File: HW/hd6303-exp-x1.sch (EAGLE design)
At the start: 40 parts, among them IC1 74HC245N, IC2 74HC245N, IC3 74HC245N, IC4 LM386N-1

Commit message: pullup for page_a13-page_a17, fixed decoder rom
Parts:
- C1, C10, C3, C4, C5, C6, C7, C8, C9: value (none) -> 100n
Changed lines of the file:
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@@
 <part name="GND10" library="supply1" library_urn="urn:adsk.eagle:library:371" deviceset="GND" device=""/>
 <part name="R3" library="resistor" library_urn="urn:adsk.eagle:library:348" deviceset="R-EU_" device="R0603" package3d_urn="urn:adsk.eagle:package:26057/1" value="10k"/>
-<part name="C4" library="rcl" deviceset="C-EU" device="C0603"/>
-<part name="C5" library="rcl" deviceset="C-EU" device="C0603"/>
-<part name="C6" library="rcl" deviceset="C-EU" device="C0603"/>
-<part name="C7" library="rcl" deviceset="C-EU" device="C0603"/>
-<part name="C8" library="rcl" deviceset="C-EU" device="C0603"/>
-<part name="C9" library="rcl" deviceset="C-EU" device="C0603"/>
-<part name="C10" library="rcl" deviceset="C-EU" device="C0603"/>
+<part name="C4" library="rcl" deviceset="C-EU" device="C0603" value="100n"/>
+<part name="C5" library="rcl" deviceset="C-EU" device="C0603" value="100n"/>
+<part name="C6" library="rcl" deviceset="C-EU" device="C0603" value="100n"/>
+<part name="C7" library="rcl" deviceset="C-EU" device="C0603" value="100n"/>
+<part name="C8" library="rcl" deviceset="C-EU" device="C0603" value="100n"/>
+<part name="C9" library="rcl" deviceset="C-EU" device="C0603" value="100n"/>
+<part name="C10" library="rcl" deviceset="C-EU" device="C0603" value="100n"/>
 <part name="GND16" library="supply1" library_urn="urn:adsk.eagle:library:371" deviceset="GND" device=""/>
 <part name="P+14" library="supply1" library_urn="urn:adsk.eagle:library:371" deviceset="VCC" device=""/>
 <part name="C12" library="resistor" library_urn="urn:adsk.eagle:library:348" deviceset="C-EU" device="C0805" package3d_urn="urn:adsk.eagle:package:26137/1" value="10uF"/>
-<part name="C1" library="rcl" deviceset="C-EU" device="C0603"/>
+<part name="C1" library="rcl" deviceset="C-EU" device="C0603" value="100n"/>
 <part name="IC4" library="linear" library_urn="urn:adsk.eagle:library:262" deviceset="LM386?-*" device="N" package3d_urn="urn:adsk.eagle:package:16409/2" technology="1"/>
 <part name="GND11" library="supply1" library_urn="urn:adsk.eagle:library:371" deviceset="GND" device=""/>
@@
 <part name="C2" library="resistor" library_urn="urn:adsk.eagle:library:348" deviceset="C-EU" device="C0805" package3d_urn="urn:adsk.eagle:package:26137/1" value="10uF"/>
 <part name="GND14" library="supply1" library_urn="urn:adsk.eagle:library:371" deviceset="GND" device=""/>
-<part name="C3" library="rcl" deviceset="C-EU" device="C0603"/>
+<part name="C3" library="rcl" deviceset="C-EU" device="C0603" value="100n"/>
 <part name="R6" library="resistor" library_urn="urn:adsk.eagle:library:348" deviceset="R-EU_" device="R0603" package3d_urn="urn:adsk.eagle:package:26057/1" value="10"/>
 <part name="GND15" library="supply1" library_urn="urn:adsk.eagle:library:371" deviceset="GND" device=""/>

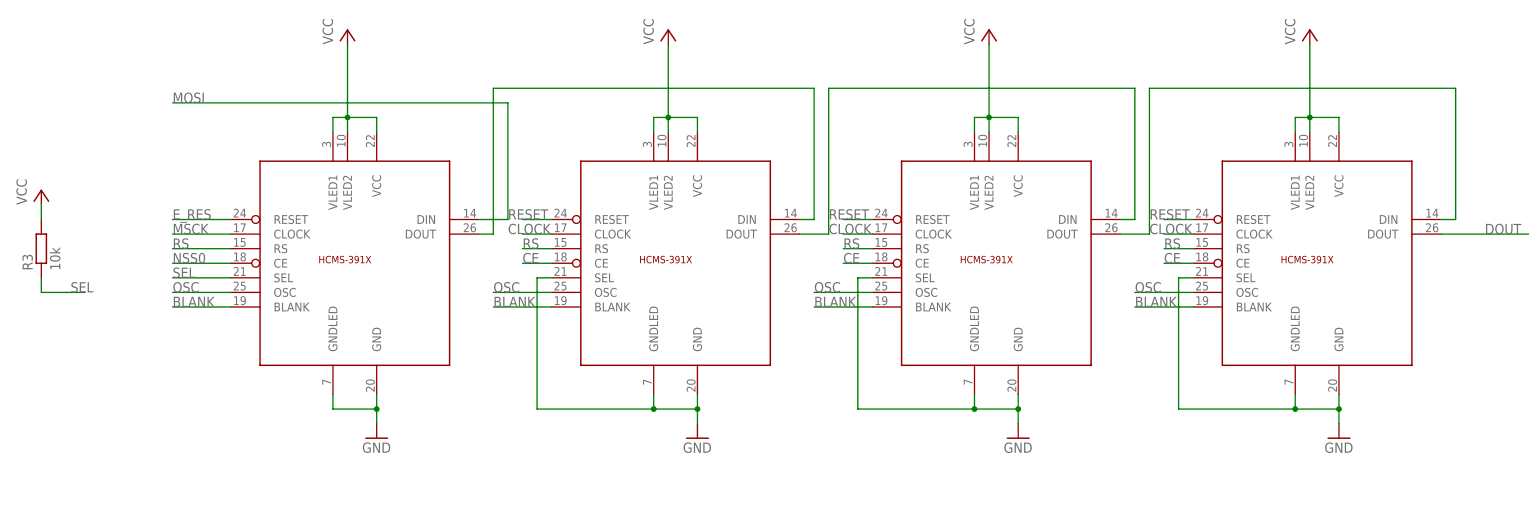
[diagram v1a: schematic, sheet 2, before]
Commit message: fixed missed nets
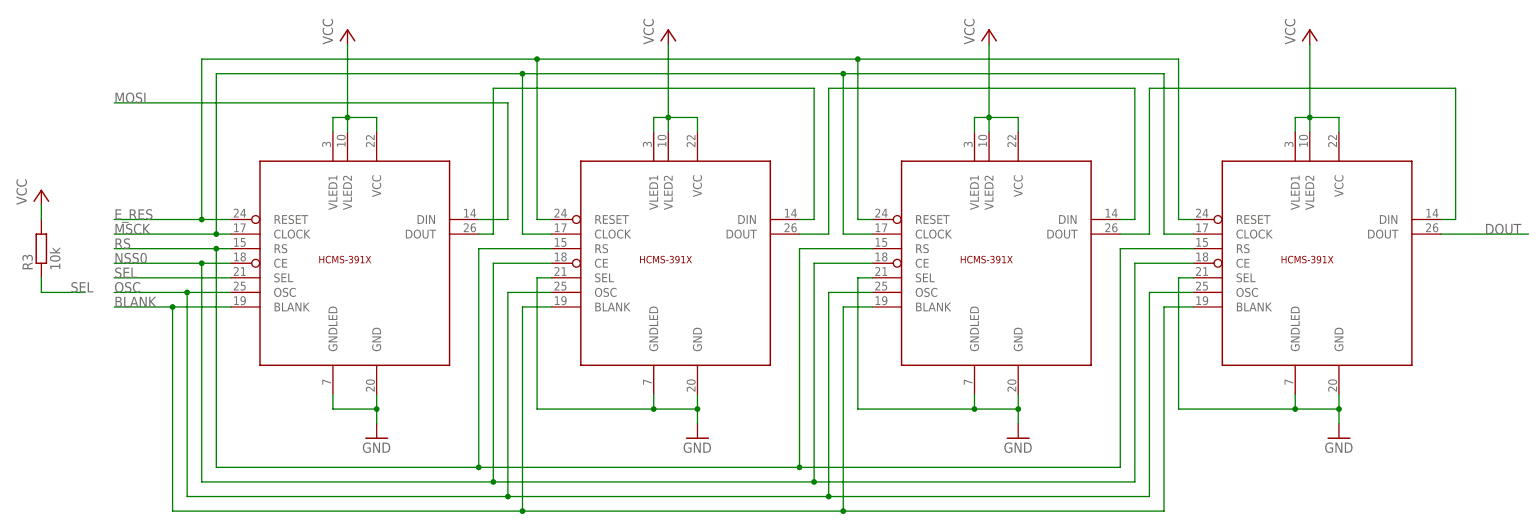
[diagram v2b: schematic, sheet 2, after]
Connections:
- removed net CE: U$2.CE, U$3.CE, U$4.CE
- removed net CLOCK: U$2.CLOCK, U$3.CLOCK, U$4.CLOCK
- removed net RESET: U$2.RESET, U$3.RESET, U$4.RESET
- net E_RES: now also U$2.RESET, U$3.RESET, U$4.RESET
- net MSCK: now also U$2.CLOCK, U$3.CLOCK, U$4.CLOCK
- net NSS0: now also U$2.CE, U$3.CE, U$4.CE

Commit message: released in pcb
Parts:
- added SPI: (no value), pinhead:PINHD-1X8
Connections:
- removed net BLANK: STEPFPGA.GPIO21, U$1.BLANK, U$2.BLANK, U$3.BLANK, U$4.BLANK
- new net NSS2: SPI.4, STEPFPGA.GPIO21
- net +5V: now also SPI.1
- net E_RES: now also SPI.3
- net GND: now also SPI.8, U$1.BLANK, U$2.BLANK, U$3.BLANK, U$4.BLANK
- net MISO: now also SPI.6
- net MOSI: now also SPI.7
- net MSCK: now also SPI.5
- net VCC: now also SPI.2
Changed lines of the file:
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@@
 <part name="UART" library="pinhead" library_urn="urn:adsk.eagle:library:325" deviceset="PINHD-1X3" device="" package3d_urn="urn:adsk.eagle:package:22458/2"/>
 <part name="GND18" library="supply1" deviceset="GND" device=""/>
+<part name="GND19" library="supply1" library_urn="urn:adsk.eagle:library:371" deviceset="GND" device=""/>
+<part name="SPI" library="pinhead" library_urn="urn:adsk.eagle:library:325" deviceset="PINHD-1X8" device="" package3d_urn="urn:adsk.eagle:package:22409/2"/>
+<part name="GND20" library="supply1" library_urn="urn:adsk.eagle:library:371" deviceset="GND" device=""/>
 </parts>
 <sheets>
@@
 <instance part="GND18" gate="1" x="35.56" y="129.54" smashed="yes">
 <attribute name="VALUE" x="33.02" y="127" size="1.778" layer="96"/>
+</instance>
+<instance part="SPI" gate="A" x="320.04" y="114.3" smashed="yes">
+<attribute name="NAME" x="313.69" y="127.635" size="1.778" layer="95"/>
+<attribute name="VALUE" x="313.69" y="101.6" size="1.778" layer="96"/>
+</instance>
+<instance part="GND20" gate="1" x="307.34" y="101.6" smashed="yes">
+<attribute name="VALUE" x="304.8" y="99.06" size="1.778" layer="96"/>
 </instance>
 </instances>
@@
 <wire x1="35.56" y1="134.62" x2="35.56" y2="132.08" width="0.1524" layer="91"/>
 </segment>
+<segment>
+<pinref part="SPI" gate="A" pin="8"/>
+<pinref part="GND20" gate="1" pin="GND"/>
+<wire x1="317.5" y1="106.68" x2="307.34" y2="106.68" width="0.1524" layer="91"/>
+<wire x1="307.34" y1="106.68" x2="307.34" y2="104.14" width="0.1524" layer="91"/>
+</segment>
 </net>
 <net name="+5V" class="0">
@@
 <wire x1="292.1" y1="43.18" x2="292.1" y2="53.34" width="0.1524" layer="91"/>
 </segment>
+<segment>
+<pinref part="SPI" gate="A" pin="1"/>
+<wire x1="317.5" y1="124.46" x2="302.26" y2="124.46" width="0.1524" layer="91"/>
+<label x="302.26" y="124.46" size="1.778" layer="95"/>
+</segment>
 </net>
 <net name="P23" class="0">
@@
 <wire x1="147.32" y1="88.9" x2="137.16" y2="88.9" width="0.1524" layer="91"/>
 <label x="137.16" y="88.9" size="1.778" layer="95"/>
+</segment>
+<segment>
+<pinref part="SPI" gate="A" pin="3"/>
+<wire x1="317.5" y1="119.38" x2="302.26" y2="119.38" width="0.1524" layer="91"/>
+<label x="302.26" y="119.38" size="1.778" layer="95"/>
 </segment>
 </net>
@@
 <wire x1="248.92" y1="-25.4" x2="248.92" y2="-30.48" width="0.1524" layer="91"/>
 </segment>
+<segment>
+<pinref part="SPI" gate="A" pin="2"/>
+<wire x1="317.5" y1="121.92" x2="302.26" y2="121.92" width="0.1524" layer="91"/>
+<label x="302.26" y="121.92" size="1.778" layer="95"/>
+</segment>
 </net>
 <net name="E_A7" class="0">
@@
 <label x="226.06" y="106.68" size="1.778" layer="95"/>
 </segment>
+<segment>
+<pinref part="SPI" gate="A" pin="7"/>
+<wire x1="317.5" y1="109.22" x2="302.26" y2="109.22" width="0.1524" layer="91"/>
+<label x="302.26" y="109.22" size="1.778" layer="95"/>
+</segment>
 </net>
 <net name="MISO" class="0">
@@
 <label x="226.06" y="93.98" size="1.778" layer="95"/>
 </segment>
+<segment>
+<pinref part="SPI" gate="A" pin="6"/>
+<wire x1="317.5" y1="111.76" x2="302.26" y2="111.76" width="0.1524" layer="91"/>
+<label x="302.26" y="111.76" size="1.778" layer="95"/>
+</segment>
 </net>
 <net name="MSCK" class="0">
@@
 <label x="226.06" y="99.06" size="1.778" layer="95"/>
 </segment>
+<segment>
+<pinref part="SPI" gate="A" pin="5"/>
+<wire x1="317.5" y1="114.3" x2="302.26" y2="114.3" width="0.1524" layer="91"/>
+<label x="302.26" y="114.3" size="1.778" layer="95"/>
+</segment>
 </net>
 <net name="NSS0" class="0">
@@
 <wire x1="259.08" y1="38.1" x2="248.92" y2="38.1" width="0.1524" layer="91"/>
 <label x="248.92" y="38.1" size="1.778" layer="95"/>
-</segment>
-</net>
-<net name="BLANK" class="0">
-<segment>
-<pinref part="STEPFPGA" gate="G$1" pin="GPIO21"/>
-<wire x1="172.72" y1="93.98" x2="185.42" y2="93.98" width="0.1524" layer="91"/>
-<label x="180.34" y="93.98" size="1.778" layer="95"/>
 </segment>
 </net>
@@
 <pinref part="C13" gate="G$1" pin="2"/>
 <wire x1="297.18" y1="30.48" x2="297.18" y2="27.94" width="0.1524" layer="91"/>
+</segment>
+</net>
+<net name="NSS2" class="0">
+<segment>
+<pinref part="STEPFPGA" gate="G$1" pin="GPIO21"/>
+<wire x1="172.72" y1="93.98" x2="185.42" y2="93.98" width="0.1524" layer="91"/>
+<label x="180.34" y="93.98" size="1.778" layer="95"/>
+</segment>
+<segment>
+<pinref part="SPI" gate="A" pin="4"/>
+<wire x1="317.5" y1="116.84" x2="302.26" y2="116.84" width="0.1524" layer="91"/>
+<label x="302.26" y="116.84" size="1.778" layer="95"/>
 </segment>
 </net>
@@
 <attribute name="NAME" x="-16.7386" y="57.15" size="1.778" layer="95" rot="R90"/>
 <attribute name="VALUE" x="-11.938" y="57.15" size="1.778" layer="96" rot="R90"/>
+</instance>
+<instance part="GND19" gate="1" x="-2.54" y="45.72" smashed="yes">
+<attribute name="VALUE" x="-5.08" y="43.18" size="1.778" layer="96"/>
 </instance>
 </instances>
@@
 <wire x1="43.18" y1="30.48" x2="43.18" y2="33.02" width="0.1524" layer="91"/>
 <junction x="43.18" y="33.02"/>
+</segment>
+<segment>
+<pinref part="U$1" gate="G$1" pin="BLANK"/>
+<wire x1="17.78" y1="50.8" x2="7.62" y2="50.8" width="0.1524" layer="91"/>
+<pinref part="U$4" gate="G$1" pin="BLANK"/>
+<wire x1="185.42" y1="50.8" x2="180.34" y2="50.8" width="0.1524" layer="91"/>
+<wire x1="180.34" y1="50.8" x2="180.34" y2="15.24" width="0.1524" layer="91"/>
+<wire x1="180.34" y1="15.24" x2="124.46" y2="15.24" width="0.1524" layer="91"/>
+<wire x1="124.46" y1="15.24" x2="68.58" y2="15.24" width="0.1524" layer="91"/>
+<wire x1="68.58" y1="15.24" x2="7.62" y2="15.24" width="0.1524" layer="91"/>
+<wire x1="7.62" y1="15.24" x2="7.62" y2="50.8" width="0.1524" layer="91"/>
+<pinref part="U$3" gate="G$1" pin="BLANK"/>
+<wire x1="129.54" y1="50.8" x2="124.46" y2="50.8" width="0.1524" layer="91"/>
+<wire x1="124.46" y1="50.8" x2="124.46" y2="15.24" width="0.1524" layer="91"/>
+<junction x="124.46" y="15.24"/>
+<pinref part="U$2" gate="G$1" pin="BLANK"/>
+<wire x1="73.66" y1="50.8" x2="68.58" y2="50.8" width="0.1524" layer="91"/>
+<wire x1="68.58" y1="50.8" x2="68.58" y2="15.24" width="0.1524" layer="91"/>
+<junction x="68.58" y="15.24"/>
+<pinref part="GND19" gate="1" pin="GND"/>
+<wire x1="7.62" y1="50.8" x2="-2.54" y2="50.8" width="0.1524" layer="91"/>
+<wire x1="-2.54" y1="50.8" x2="-2.54" y2="48.26" width="0.1524" layer="91"/>
+<junction x="7.62" y="50.8"/>
 </segment>
 </net>
@@
 </segment>
 </net>
-<net name="BLANK" class="0">
-<segment>
-<pinref part="U$1" gate="G$1" pin="BLANK"/>
-<wire x1="17.78" y1="50.8" x2="7.62" y2="50.8" width="0.1524" layer="91"/>
-<label x="-2.54" y="50.8" size="1.778" layer="95"/>
-<pinref part="U$4" gate="G$1" pin="BLANK"/>
-<wire x1="7.62" y1="50.8" x2="-2.54" y2="50.8" width="0.1524" layer="91"/>
-<wire x1="185.42" y1="50.8" x2="180.34" y2="50.8" width="0.1524" layer="91"/>
-<wire x1="180.34" y1="50.8" x2="180.34" y2="15.24" width="0.1524" layer="91"/>
-<wire x1="180.34" y1="15.24" x2="124.46" y2="15.24" width="0.1524" layer="91"/>
-<wire x1="124.46" y1="15.24" x2="68.58" y2="15.24" width="0.1524" layer="91"/>
-<wire x1="68.58" y1="15.24" x2="7.62" y2="15.24" width="0.1524" layer="91"/>
-<wire x1="7.62" y1="15.24" x2="7.62" y2="50.8" width="0.1524" layer="91"/>
-<junction x="7.62" y="50.8"/>
-<pinref part="U$3" gate="G$1" pin="BLANK"/>
-<wire x1="129.54" y1="50.8" x2="124.46" y2="50.8" width="0.1524" layer="91"/>
-<wire x1="124.46" y1="50.8" x2="124.46" y2="15.24" width="0.1524" layer="91"/>
-<junction x="124.46" y="15.24"/>
-<pinref part="U$2" gate="G$1" pin="BLANK"/>
-<wire x1="73.66" y1="50.8" x2="68.58" y2="50.8" width="0.1524" layer="91"/>
-<wire x1="68.58" y1="50.8" x2="68.58" y2="15.24" width="0.1524" layer="91"/>
-<junction x="68.58" y="15.24"/>
-</segment>
-</net>

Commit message: fix
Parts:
- added C14, C15, C16, C17: 100n, rcl:C-EUC0603
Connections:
- net +5V: now also C14.1, C15.1, C16.1, C17.1, U$1.VLED1, U$1.VLED2, U$2.VLED1, U$2.VLED2, U$3.VLED1, U$3.VLED2, U$4.VLED1, U$4.VLED2
- net GND: now also C14.2, C15.2, C16.2, C17.2
- net VCC: no longer U$1.VLED1, U$1.VLED2, U$2.VLED1, U$2.VLED2, U$3.VLED1, U$3.VLED2, U$4.VLED1, U$4.VLED2
